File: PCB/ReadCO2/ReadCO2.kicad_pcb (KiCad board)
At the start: 2 copper layers, 30 x 131.3 mm, 9 parts, among them J1 Conn_01x05, J2 Conn_01x03, J3 Conn_01x04

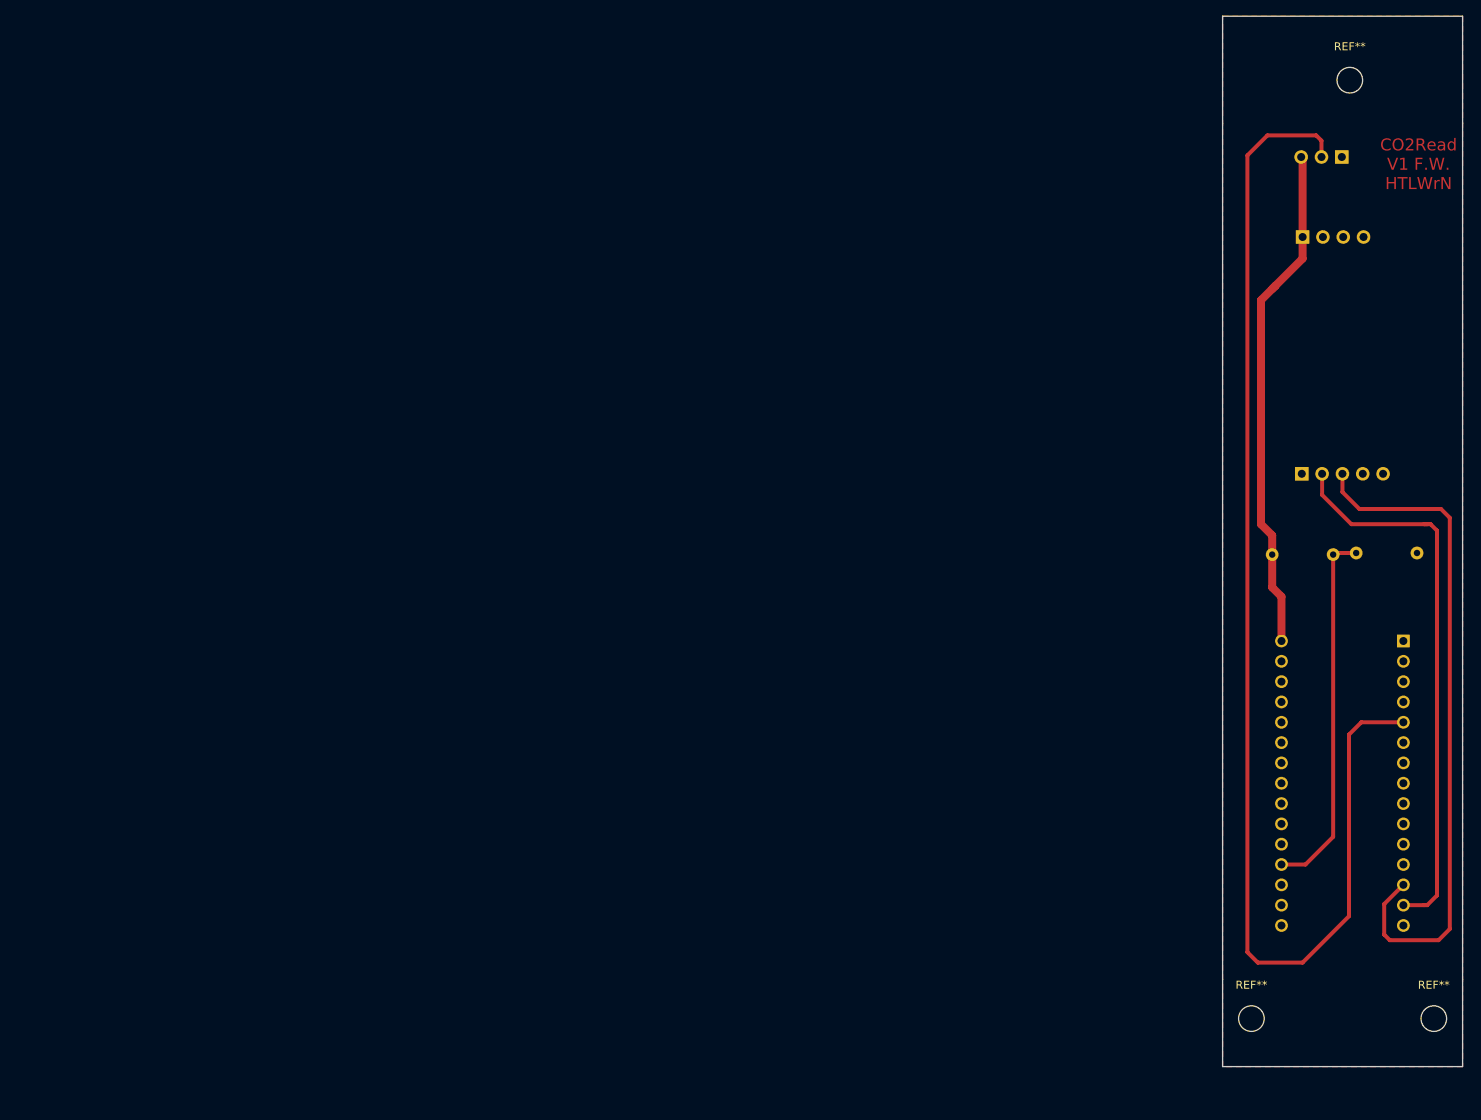
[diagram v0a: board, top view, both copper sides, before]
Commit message: edited PCB
edited pcb layout to fit Eckers case idea
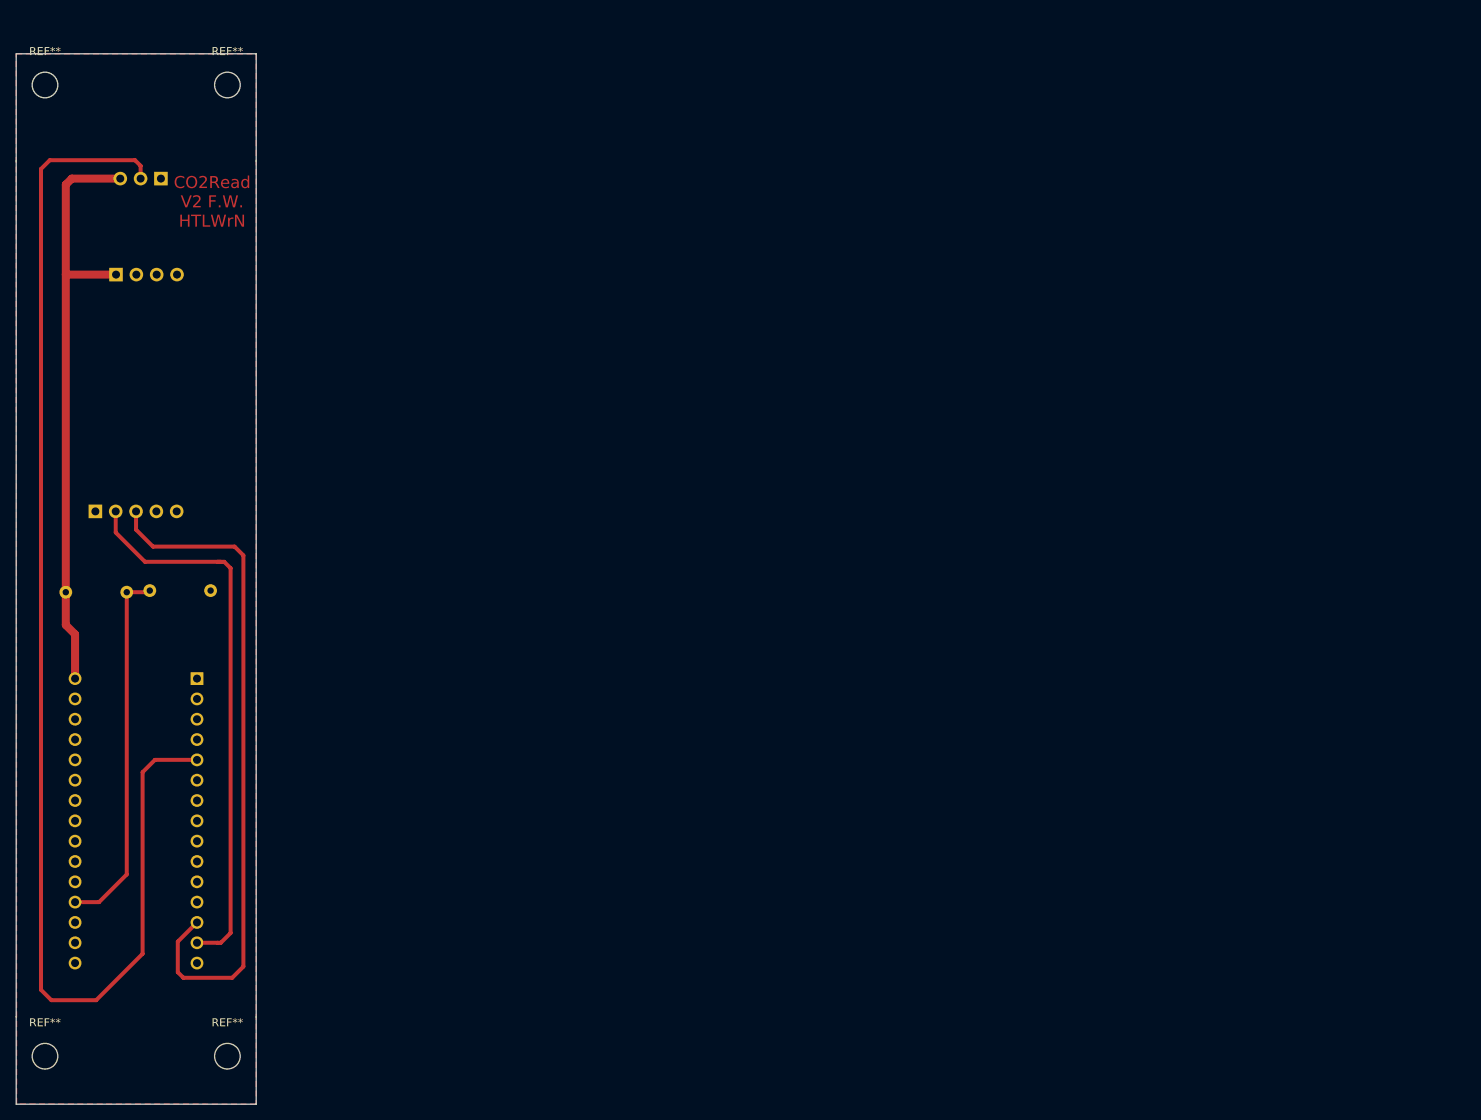
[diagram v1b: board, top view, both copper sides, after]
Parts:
- removed the REF** at (235.9, 34.6)
- added REF**: MountingHole_3.2mm_M3, MountingHole:MountingHole_3.2mm_M3, F.Cu at (72.8, 35.2)
- added REF**: MountingHole_3.2mm_M3, MountingHole:MountingHole_3.2mm_M3, F.Cu at (95.6, 35.2)
- moved A1 150.9 mm to (91.8, 109.4)
- moved J1 150.9 mm to (79.1, 88.5)
- moved REF** 150.9 mm to (95.6, 156.6)
- moved REF** 150.9 mm to (72.8, 156.6)
- moved R1 150.9 mm to (75.4, 98.6)
- moved R2 150.9 mm to (85.9, 98.4)
- moved J3 148.4 mm to (81.7, 58.9)
- moved J2 147.6 mm to (87.3, 46.9)
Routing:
- net +5V: track 64.4 -> 75.6 mm
- net LED_DIn: track 158.0 -> 163.2 mm
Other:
- board text added: "CO2Read V2 F.W. HTLWrN"
- board text removed: "CO2Read V1 F.W. HTLWrN"
